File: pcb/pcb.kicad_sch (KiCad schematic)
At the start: 18 parts

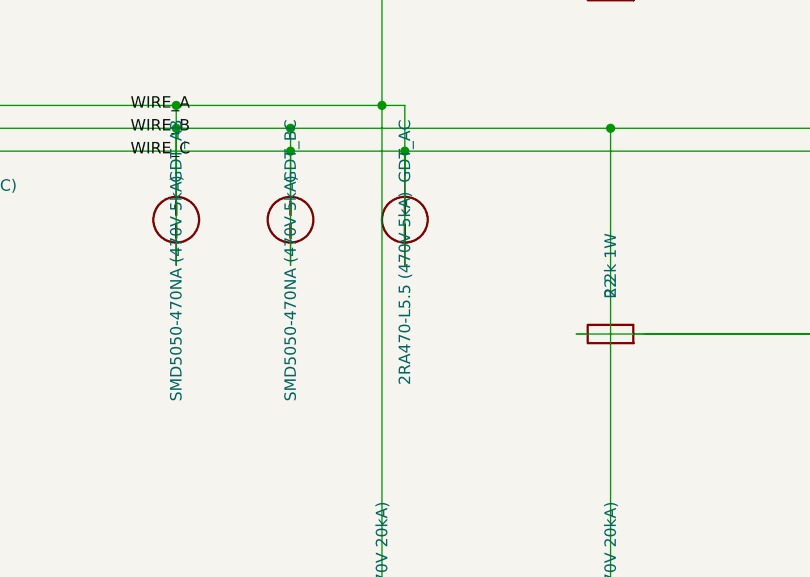
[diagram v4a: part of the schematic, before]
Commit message: Review component assignments in light of JLCPCB stock availability
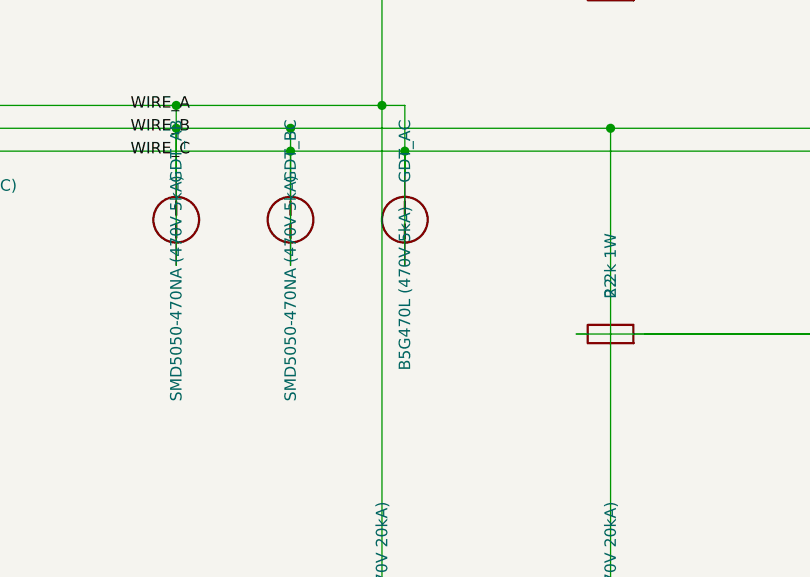
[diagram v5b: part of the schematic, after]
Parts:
- GDT_AC: value 2RA470-L5.5 (470V 5kA) -> B5G470L (470V 5kA); LCSC C52741208 -> C5337217; MPN 2RA470-L5.5 -> B5G470L
- GDT_A_E, GDT_B_E, GDT_C_E: LCSC C434855 -> C2836978
- J_EARTH, J_IN: LCSC ASSIGN_BY_JLCPCB -> C474957
- R1, R2: LCSC ASSIGN_BY_JLCPCB -> C1368610; MPN MFR01SF2201A10 -> MBE04140C2201FC100
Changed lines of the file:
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@@
 			(effects (font (size 1.27 1.27)) hide)
 		)
-		(property "LCSC" "ASSIGN_BY_JLCPCB" (at 38.1 63.5 0)
+		(property "LCSC" "C474957" (at 38.1 63.5 0)
 			(effects (font (size 1.27 1.27)) hide)
 		)
@@
 			(effects (font (size 1.27 1.27)) hide)
 		)
-		(property "LCSC" "ASSIGN_BY_JLCPCB" (at 38.1 127 0)
+		(property "LCSC" "C474957" (at 38.1 127 0)
 			(effects (font (size 1.27 1.27)) hide)
 		)
@@
 			(effects (font (size 1.27 1.27)) hide)
 		)
-		(property "MPN" "MFR01SF2201A10" (at 114.3 50.8 0)
-			(effects (font (size 1.27 1.27)) hide)
-		)
-		(property "LCSC" "ASSIGN_BY_JLCPCB" (at 114.3 50.8 0)
+		(property "MPN" "MBE04140C2201FC100" (at 114.3 50.8 0)
+			(effects (font (size 1.27 1.27)) hide)
+		)
+		(property "LCSC" "C1368610" (at 114.3 50.8 0)
 			(effects (font (size 1.27 1.27)) hide)
 		)
@@
 			(effects (font (size 1.27 1.27)) hide)
 		)
-		(property "MPN" "MFR01SF2201A10" (at 114.3 88.9 0)
-			(effects (font (size 1.27 1.27)) hide)
-		)
-		(property "LCSC" "ASSIGN_BY_JLCPCB" (at 114.3 88.9 0)
+		(property "MPN" "MBE04140C2201FC100" (at 114.3 88.9 0)
+			(effects (font (size 1.27 1.27)) hide)
+		)
+		(property "LCSC" "C1368610" (at 114.3 88.9 0)
 			(effects (font (size 1.27 1.27)) hide)
 		)
@@
 			(effects (font (size 1.27 1.27)))
 		)
-		(property "Value" "2RA470-L5.5 (470V 5kA)" (at 91.44 83.82 0)
+		(property "Value" "B5G470L (470V 5kA)" (at 91.44 83.82 0)
 			(effects (font (size 1.27 1.27)))
 		)
@@
 			(effects (font (size 1.27 1.27)) hide)
 		)
-		(property "MPN" "2RA470-L5.5" (at 91.44 76.2 0)
-			(effects (font (size 1.27 1.27)) hide)
-		)
-		(property "LCSC" "C52741208" (at 91.44 76.2 0)
+		(property "MPN" "B5G470L" (at 91.44 76.2 0)
+			(effects (font (size 1.27 1.27)) hide)
+		)
+		(property "LCSC" "C5337217" (at 91.44 76.2 0)
 			(effects (font (size 1.27 1.27)) hide)
 		)
@@
 			(effects (font (size 1.27 1.27)) hide)
 		)
-		(property "LCSC" "C434855" (at 88.9 127 0)
+		(property "LCSC" "C2836978" (at 88.9 127 0)
 			(effects (font (size 1.27 1.27)) hide)
 		)
@@
 			(effects (font (size 1.27 1.27)) hide)
 		)
-		(property "LCSC" "C434855" (at 114.3 127 0)
+		(property "LCSC" "C2836978" (at 114.3 127 0)
 			(effects (font (size 1.27 1.27)) hide)
 		)
@@
 			(effects (font (size 1.27 1.27)) hide)
 		)
-		(property "LCSC" "C434855" (at 139.7 127 0)
-			(effects (font (size 1.27 1.27)) hide)
-		)
+		(property "LCSC" "C2836978" (at 139.7 127 0)
+			(effects (font (size 1.27 1.27)) hide)
+		)

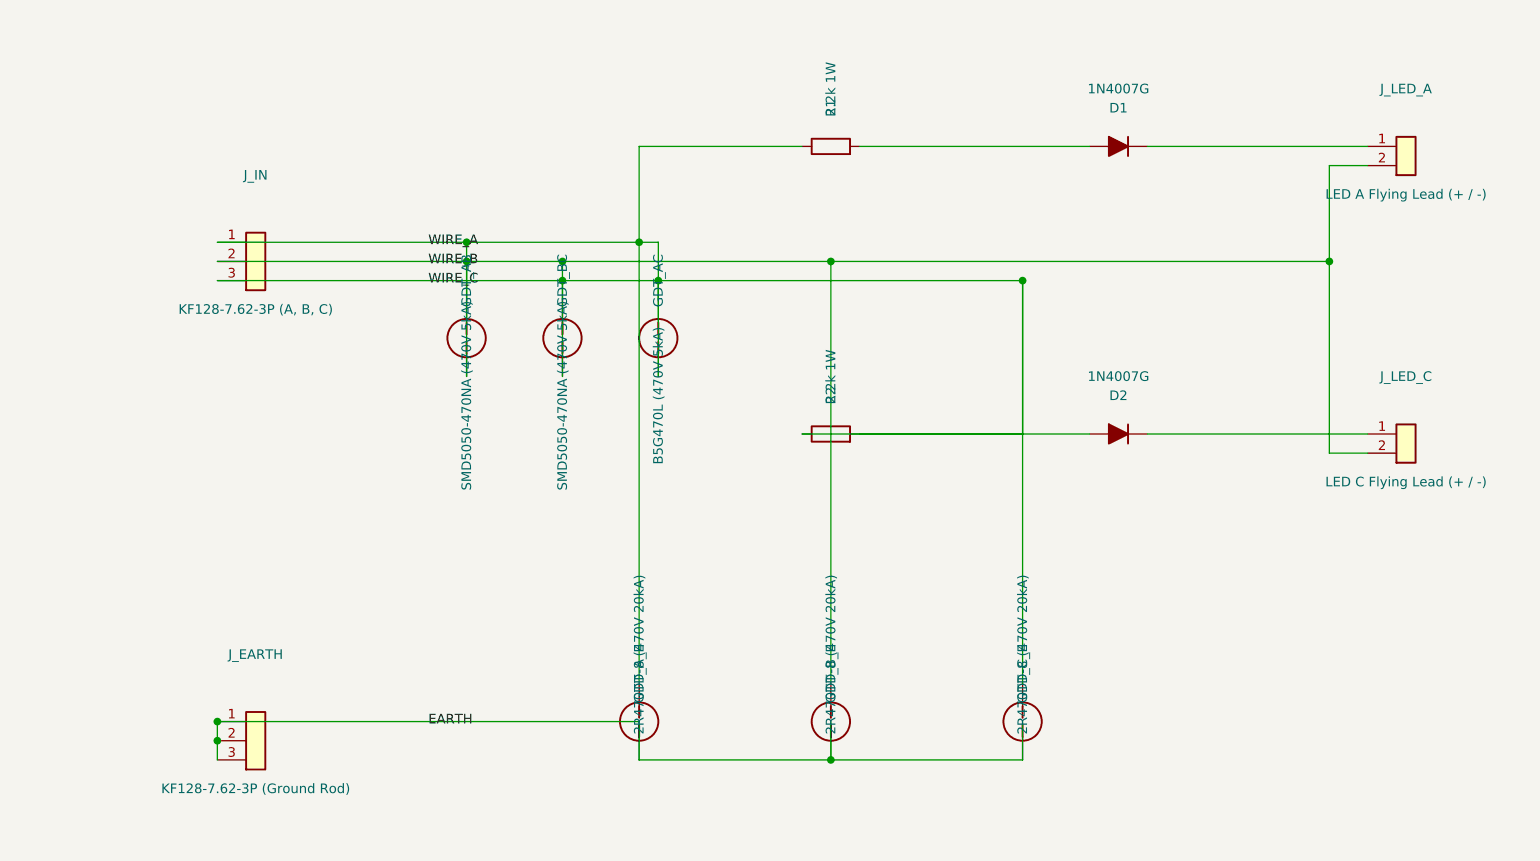
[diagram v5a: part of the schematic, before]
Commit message: Clean up schematic to align with PCB
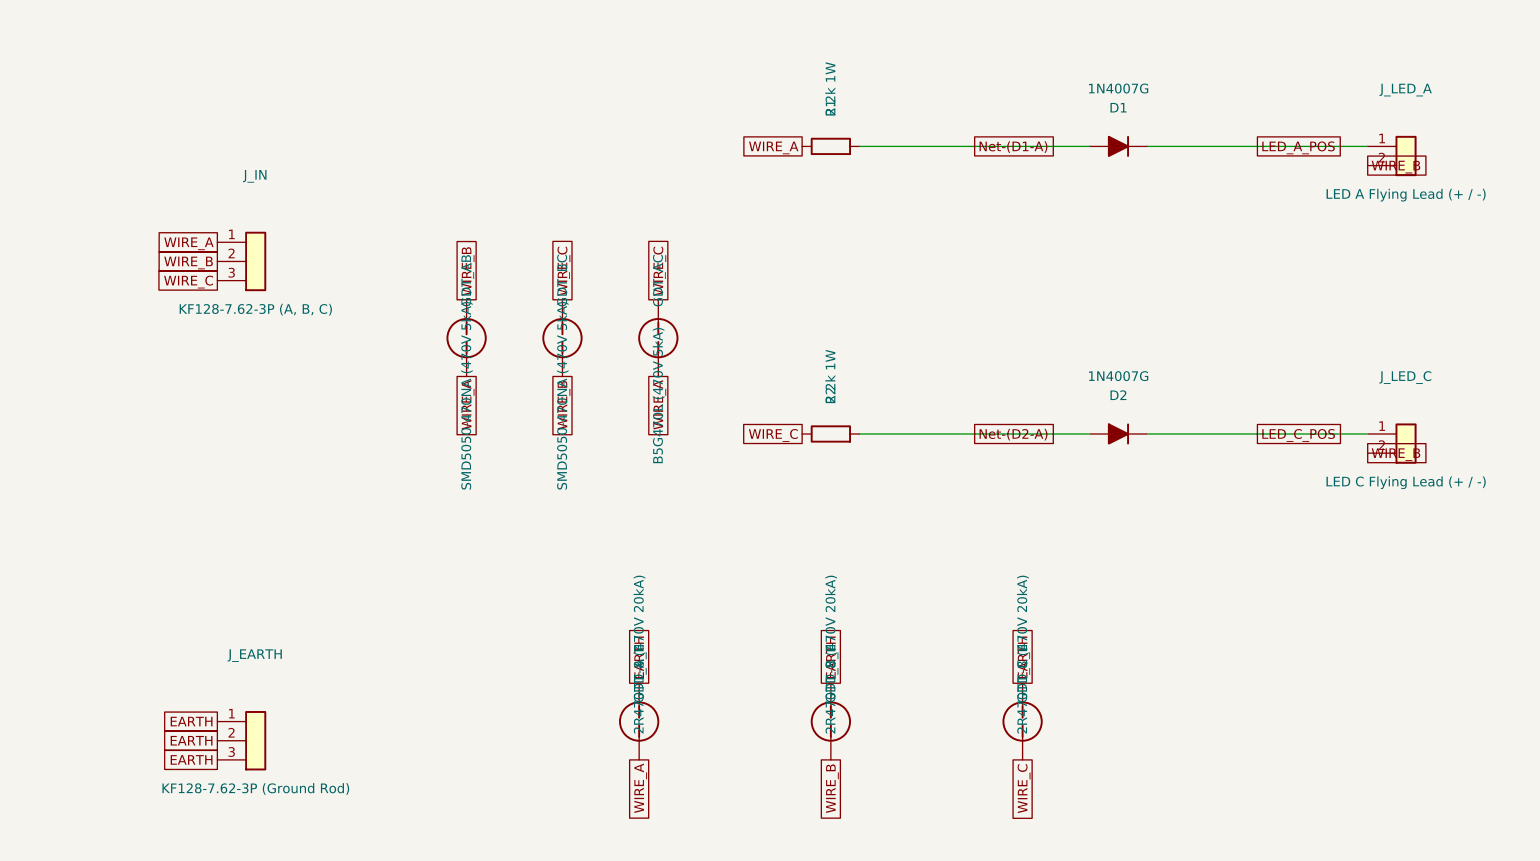
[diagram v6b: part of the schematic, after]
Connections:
- net EARTH: now also GDT_A_E.2, GDT_B_E.2, GDT_C_E.2; no longer GDT_A_E.1, GDT_B_E.1, GDT_C_E.1
- net WIRE_A: now also GDT_A_E.1; no longer D2.2 (A), GDT_AB.2, GDT_AC.2, GDT_A_E.2, GDT_BC.1, GDT_BC.2, GDT_B_E.2, GDT_C_E.2, J_IN.2 (Pin_2), J_IN.3 (Pin_3), J_LED_A.2 (Pin_2), J_LED_C.2 (Pin_2), R2.1, R2.2
- net LED_C_POS: now reaches D2.1 (K), J_LED_C.1 (Pin_1)
- net LED_A_POS: now reaches D1.1 (K), J_LED_A.1 (Pin_1)
- net Net-(D1-A): now reaches D1.2 (A), R1.2
- new net Net-(D2-A): D2.2 (A), R2.2
- new net WIRE_B: GDT_AB.2, GDT_BC.1, GDT_B_E.1, J_IN.2 (Pin_2), J_LED_A.2 (Pin_2), J_LED_C.2 (Pin_2)
- new net WIRE_C: GDT_AC.2, GDT_BC.2, GDT_C_E.1, J_IN.3 (Pin_3), R2.1
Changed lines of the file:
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@@
 		)
-	)
-	(wire (pts (xy 33.02 63.5) (xy 66.04 63.5))
-		(stroke (width 0) (type default))
-	)
-	(wire (pts (xy 66.04 63.5) (xy 66.04 71.12))
-		(stroke (width 0) (type default))
-	)
-	(wire (pts (xy 66.04 63.5) (xy 88.9 63.5))
-		(stroke (width 0) (type default))
-	)
-	(junction (at 66.04 63.5) (diameter 1.016) (color 0 0 0 0))
-	(wire (pts (xy 88.9 63.5) (xy 91.44 63.5))
-		(stroke (width 0) (type default))
-	)
-	(wire (pts (xy 91.44 63.5) (xy 91.44 71.12))
-		(stroke (width 0) (type default))
-	)
-	(junction (at 88.9 63.5) (diameter 1.016) (color 0 0 0 0))
-	(wire (pts (xy 88.9 63.5) (xy 88.9 50.8))
-		(stroke (width 0) (type default))
-	)
-	(wire (pts (xy 88.9 50.8) (xy 110.49 50.8))
-		(stroke (width 0) (type default))
-	)
-	(wire (pts (xy 88.9 63.5) (xy 88.9 121.92))
-		(stroke (width 0) (type default))
 	)
 	(wire (pts (xy 118.11 50.8) (xy 148.59 50.8))
 		(stroke (width 0) (type default))
 	)
+	(global_label "Net-(D1-A)" (at 133.35 50.8 0) (fields_autoplaced yes)
+		(effects (font (size 1.27 1.27)))
+	)
 	(wire (pts (xy 156.21 50.8) (xy 185.42 50.8))
 		(stroke (width 0) (type default))
 	)
-	(wire (pts (xy 33.02 66.04) (xy 66.04 66.04))
+	(global_label "LED_A_POS" (at 170.81 50.8 0) (fields_autoplaced yes)
+		(effects (font (size 1.27 1.27)))
+	)
+	(wire (pts (xy 118.11 88.9) (xy 148.59 88.9))
 		(stroke (width 0) (type default))
 	)
-	(wire (pts (xy 66.04 66.04) (xy 66.04 81.28))
-		(stroke (width 0) (type default))
-	)
-	(wire (pts (xy 66.04 66.04) (xy 78.74 66.04))
-		(stroke (width 0) (type default))
-	)
-	(junction (at 66.04 66.04) (diameter 1.016) (color 0 0 0 0))
-	(wire (pts (xy 78.74 66.04) (xy 78.74 71.12))
-		(stroke (width 0) (type default))
-	)
-	(wire (pts (xy 78.74 66.04) (xy 114.3 66.04))
-		(stroke (width 0) (type default))
-	)
-	(junction (at 78.74 66.04) (diameter 1.016) (color 0 0 0 0))
-	(wire (pts (xy 114.3 66.04) (xy 114.3 121.92))
-		(stroke (width 0) (type default))
-	)
-	(junction (at 114.3 66.04) (diameter 1.016) (color 0 0 0 0))
-	(wire (pts (xy 114.3 66.04) (xy 180.34 66.04))
-		(stroke (width 0) (type default))
-	)
-	(wire (pts (xy 180.34 66.04) (xy 180.34 53.34))
-		(stroke (width 0) (type default))
-	)
-	(wire (pts (xy 180.34 53.34) (xy 185.42 53.34))
-		(stroke (width 0) (type default))
-	)
-	(wire (pts (xy 180.34 66.04) (xy 180.34 91.44))
-		(stroke (width 0) (type default))
-	)
-	(junction (at 180.34 66.04) (diameter 1.016) (color 0 0 0 0))
-	(wire (pts (xy 180.34 91.44) (xy 185.42 91.44))
-		(stroke (width 0) (type default))
-	)
-	(wire (pts (xy 33.02 68.58) (xy 78.74 68.58))
-		(stroke (width 0) (type default))
-	)
-	(wire (pts (xy 78.74 68.58) (xy 78.74 81.28))
-		(stroke (width 0) (type default))
-	)
-	(wire (pts (xy 78.74 68.58) (xy 91.44 68.58))
-		(stroke (width 0) (type default))
-	)
-	(junction (at 78.74 68.58) (diameter 1.016) (color 0 0 0 0))
-	(wire (pts (xy 91.44 68.58) (xy 91.44 81.28))
-		(stroke (width 0) (type default))
-	)
-	(wire (pts (xy 91.44 68.58) (xy 139.7 68.58))
-		(stroke (width 0) (type default))
-	)
-	(junction (at 91.44 68.58) (diameter 1.016) (color 0 0 0 0))
-	(wire (pts (xy 139.7 68.58) (xy 139.7 88.9))
-		(stroke (width 0) (type default))
-	)
-	(wire (pts (xy 139.7 88.9) (xy 110.49 88.9))
-		(stroke (width 0) (type default))
-	)
-	(wire (pts (xy 139.7 68.58) (xy 139.7 121.92))
-		(stroke (width 0) (type default))
-	)
-	(junction (at 139.7 68.58) (diameter 1.016) (color 0 0 0 0))
-	(wire (pts (xy 118.11 88.9) (xy 148.59 88.9))
-		(stroke (width 0) (type default))
+	(global_label "Net-(D2-A)" (at 133.35 88.9 0) (fields_autoplaced yes)
+		(effects (font (size 1.27 1.27)))
 	)
 	(wire (pts (xy 156.21 88.9) (xy 185.42 88.9))
 		(stroke (width 0) (type default))
 	)
-	(wire (pts (xy 33.02 127) (xy 33.02 129.54))
-		(stroke (width 0) (type default))
-	)
-	(wire (pts (xy 33.02 129.54) (xy 33.02 132.08))
-		(stroke (width 0) (type default))
-	)
-	(wire (pts (xy 33.02 127) (xy 88.9 127))
-		(stroke (width 0) (type default))
-	)
-	(junction (at 33.02 127) (diameter 1.016) (color 0 0 0 0))
-	(junction (at 33.02 129.54) (diameter 1.016) (color 0 0 0 0))
-	(wire (pts (xy 88.9 127) (xy 88.9 132.08))
-		(stroke (width 0) (type default))
-	)
-	(wire (pts (xy 88.9 132.08) (xy 114.3 132.08))
-		(stroke (width 0) (type default))
-	)
-	(wire (pts (xy 114.3 132.08) (xy 139.7 132.08))
-		(stroke (width 0) (type default))
-	)
-	(wire (pts (xy 114.3 127) (xy 114.3 132.08))
-		(stroke (width 0) (type default))
-	)
-	(junction (at 114.3 132.08) (diameter 1.016) (color 0 0 0 0))
-	(wire (pts (xy 139.7 127) (xy 139.7 132.08))
-		(stroke (width 0) (type default))
-	)
-	(label "WIRE_A" (at 60.96 63.5 0) (fields_autoplaced yes)
+	(global_label "LED_C_POS" (at 170.81 88.9 0) (fields_autoplaced yes)
 		(effects (font (size 1.27 1.27)))
 	)
-	(label "WIRE_B" (at 60.96 66.04 0) (fields_autoplaced yes)
+	(global_label "WIRE_A" (at 33.02 63.5 180) (fields_autoplaced yes)
 		(effects (font (size 1.27 1.27)))
 	)
-	(label "WIRE_C" (at 60.96 68.58 0) (fields_autoplaced yes)
+	(global_label "WIRE_B" (at 33.02 66.04 180) (fields_autoplaced yes)
 		(effects (font (size 1.27 1.27)))
 	)
-	(label "EARTH" (at 60.96 127 0) (fields_autoplaced yes)
+	(global_label "WIRE_C" (at 33.02 68.58 180) (fields_autoplaced yes)
 		(effects (font (size 1.27 1.27)))
 	)
+	(global_label "EARTH" (at 33.02 127.0 180) (fields_autoplaced yes)
+		(effects (font (size 1.27 1.27)))
+	)
+	(global_label "EARTH" (at 33.02 129.54 180) (fields_autoplaced yes)
+		(effects (font (size 1.27 1.27)))
+	)
+	(global_label "EARTH" (at 33.02 132.08 180) (fields_autoplaced yes)
+		(effects (font (size 1.27 1.27)))
+	)
+	(global_label "WIRE_A" (at 110.49 50.8 180) (fields_autoplaced yes)
+		(effects (font (size 1.27 1.27)))
+	)
+	(global_label "WIRE_B" (at 185.42 53.34 0) (fields_autoplaced yes)
+		(effects (font (size 1.27 1.27)))
+	)
+	(global_label "WIRE_C" (at 110.49 88.9 180) (fields_autoplaced yes)
+		(effects (font (size 1.27 1.27)))
+	)
+	(global_label "WIRE_B" (at 185.42 91.44 0) (fields_autoplaced yes)
+		(effects (font (size 1.27 1.27)))
+	)
+	(global_label "WIRE_A" (at 66.04 81.28 270) (fields_autoplaced yes)
+		(effects (font (size 1.27 1.27)))
+	)
+	(global_label "WIRE_B" (at 66.04 71.12 90) (fields_autoplaced yes)
+		(effects (font (size 1.27 1.27)))
+	)
+	(global_label "WIRE_B" (at 78.74 81.28 270) (fields_autoplaced yes)
+		(effects (font (size 1.27 1.27)))
+	)
+	(global_label "WIRE_C" (at 78.74 71.12 90) (fields_autoplaced yes)
+		(effects (font (size 1.27 1.27)))
+	)
+	(global_label "WIRE_A" (at 91.44 81.28 270) (fields_autoplaced yes)
+		(effects (font (size 1.27 1.27)))
+	)
+	(global_label "WIRE_C" (at 91.44 71.12 90) (fields_autoplaced yes)
+		(effects (font (size 1.27 1.27)))
+	)
+	(global_label "WIRE_A" (at 88.90 132.08 270) (fields_autoplaced yes)
+		(effects (font (size 1.27 1.27)))
+	)
+	(global_label "EARTH" (at 88.90 121.92 90) (fields_autoplaced yes)
+		(effects (font (size 1.27 1.27)))
+	)
+	(global_label "WIRE_B" (at 114.30 132.08 270) (fields_autoplaced yes)
+		(effects (font (size 1.27 1.27)))
+	)
+	(global_label "EARTH" (at 114.30 121.92 90) (fields_autoplaced yes)
+		(effects (font (size 1.27 1.27)))
+	)
+	(global_label "WIRE_C" (at 139.70 132.08 270) (fields_autoplaced yes)
+		(effects (font (size 1.27 1.27)))
+	)
+	(global_label "EARTH" (at 139.70 121.92 90) (fields_autoplaced yes)
+		(effects (font (size 1.27 1.27)))
+	)

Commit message: Clean up schematic for visual clarity and overlaps
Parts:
- GDT_AB, GDT_BC: value SMD5050-470NA (470V 5kA) -> SMD5050-470NA
- GDT_AC: value B5G470L (470V 5kA) -> B5G470L
- GDT_A_E, GDT_B_E, GDT_C_E: value 2R470TD-8 (470V 20kA) -> 2R470TD-8
- H1, H2, H3, H4: value MountingHole_3.2mm_M3 -> 3.2mm M3
- J_IN: value KF128-7.62-3P (A, B, C) -> KF128-7.62-3P
- J_LED_A: value LED A Flying Lead (+ / -) -> KF129-5.08-2P
- J_LED_C: value LED C Flying Lead (+ / -) -> KF129-5.08-2P
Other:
- note added: "(>=2.0mm air gap standoff)"
- note added: "1. RF RUN MODE (Transmitter Active): 4-10 kHz AC carrier. GDT capacitance <1.5pF (RF transparent). Diodes D1/D2 block reverse flow."
- note added: "2. DC TEST MODE (Fault Finding): Disconnect RF transmitter; inject +36V DC on Wires A & C with Wire B as DC 0V return. ~15mA/LED."
- note added: "3. SURGE SUPPRESSION: GDT_AB/BC/AC clamp 5kA differential pulses; GDT_A/B/C_E divert 20kA lightning to Earth bus & ground rods."
- note added: "4km 3-Core DogWatch SmartFence Diagnostic Milestone & 20kA Grounding Unit"
- note added: "Axial GDT bridges over Wire B"
- note added: "CIRCUIT THEORY & OPERATIONAL MODES:"
- note added: "CORE-TO-CORE DIFFERENTIAL SURGE (5kA)"
- note added: "DIAGNOSTIC TEST INDICATORS (+36V DC TEST MODE)"
- note added: "DOG FENCE INDICATOR & SURGE PROTECTION SYSTEM (v1.1.0)"
- note added: "LINE-TO-EARTH SURGE (20kA)"
- note added: "MECHANICAL FIXTURES"
- note added: "SOLID 4.5mm EARTH BUS (2 oz Top + 2 oz Bottom Cu, 5x Heavy Stitching Vias)"
- moved on the sheet: D1, D2, GDT_AB, GDT_AC, GDT_A_E, GDT_BC, GDT_B_E, GDT_C_E, H1, H2, H3, H4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
